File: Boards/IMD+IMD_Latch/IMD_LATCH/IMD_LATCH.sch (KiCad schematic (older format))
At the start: 28 parts

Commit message: hopefully one of the last schematic pushes
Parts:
- removed C?: C_22uF, footprints:C_1206_OEM, symbol Formula:C_22uF
- removed R? (x2): R_604K, footprints:R_0805_OEM, symbol Formula:R_604K
- removed R? (x2): R_2.2K, footprints:R_0805_OEM, symbol Formula:R_2.2K
- removed R?: R_300K, footprints:R_0805_OEM, symbol Formula:R_300K
- removed U?: TLV3701QDBVRG4Q1, footprints:SOT-23-5_OEM, symbol Formula:TLV3701QDBVRG4Q1
- added C1: C_2.2uF, footprints:C_0603_1608Metric, symbol formula:C_2.2uF
- added J1: UF_5_VT, symbol formula:UF_5_VT
- added R7: R_1.82M, footprints:R_0805_OEM, symbol formula:R_1.82M
- C2: renamed from C?; symbol Formula:C_10uF_16V -> IMD_LATCH-rescue:C_10uF_16V-Formula
- D1: renamed from D?; symbol Formula:D_Zener_18V -> IMD_LATCH-rescue:D_Zener_18V-Formula
- D2, D4: renamed from D?; symbol Formula:LED_0805 -> IMD_LATCH-rescue:LED_0805-Formula
- F1: renamed from F?; symbol Formula:F_500mA_16V -> IMD_LATCH-rescue:F_500mA_16V-Formula
- J2: renamed from J?; symbol Formula:MM_F_RA_04 -> IMD_LATCH-rescue:MM_F_RA_04-Formula
- J3: renamed from J?; symbol Formula:MicroFit_V_2 -> IMD_LATCH-rescue:MicroFit_V_2-Formula
- K1: renamed from K?; symbol Formula:G5Q-1A4-DC5-5V -> IMD_LATCH-rescue:G5Q-1A4-DC5-5V-Formula
- Q1, Q2: renamed from Q?; symbol Formula:SSM3K333R -> IMD_LATCH-rescue:SSM3K333R-Formula
- R1: renamed from R?; symbol Formula:R_2.2K -> IMD_LATCH-rescue:R_2.2K-Formula
- R2: renamed from R?; symbol Formula:R_300K -> IMD_LATCH-rescue:R_300K-Formula
- R3, R8: renamed from R?; symbol Formula:R_604K -> IMD_LATCH-rescue:R_604K-Formula
- R4, R5, R9: renamed from R?; symbol Formula:R_1K -> IMD_LATCH-rescue:R_1K-Formula
- R6: renamed from R?; symbol Formula:R_120K -> IMD_LATCH-rescue:R_120K-Formula
- U1: renamed from U?; symbol Formula:TLV3701QDBVRG4Q1 -> IMD_LATCH-rescue:TLV3701QDBVRG4Q1-Formula
- U2: renamed from U?; symbol Formula:CD4043BPWR -> IMD_LATCH-rescue:CD4043BPWR-Formula
- gave numbers to parts that had none: 1
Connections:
- net labels added: IMD_Output
- net labels removed: imd_side_out
- wire segments 79 -> 68
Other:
- note removed: "8V Output"
- note removed: "IMD Output\n"
- moved on the sheet: U1

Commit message: Begin Layout
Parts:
- removed U2: CD4043BPWR, footprints:TSSOP-16-OEM, symbol IMD_LATCH-rescue:CD4043BPWR-Formula
- added C3, C4: C_0.1uF, footprints:C_0805_OEM, symbol footprints:C_0.1uF
- added R10: R_2.2K, footprints:R_0805_OEM, symbol formula:R_2.2K
- added R11: R_2.2K, footprints:R_0805_OEM, symbol IMD_LATCH-rescue:R_2.2K-Formula
- added R12: R_300K, footprints:R_0805_OEM, symbol IMD_LATCH-rescue:R_300K-Formula
- added R13: R_604K, footprints:R_0805_OEM, symbol IMD_LATCH-rescue:R_604K-Formula
- added U2: CD4043BPWR, footprints:TSSOP-16-OEM, symbol formula:CD4043BPWR
- added U3: TLV3701QDBVRG4Q1, footprints:SOT-23-5_OEM, symbol formula:TLV3701QDBVRG4Q1
- D3: footprint (none) -> footprints:D_0805_OEM
- J1: footprint (none) -> footprints:Ultrafit_5
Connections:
- net +12V: no longer D1.1 (K)
- net 12V_Fused: now also D1.1 (K), C3.2, C4.2, R11.2, U2.16 (Vdd), U2.5 (ENABLE), U3.5 (V+)
- net GND: now also C3.1, C4.1, R10.2, R13.1, U2.11 (R3), U2.12 (S3), U2.14 (S4), U2.15 (R4), U2.6 (S2), U2.7 (R2), U2.8 (Vss), U3.2 (V-)
- net IMD_Output: now also R10.1, U3.1 (+)
- net IMD_Status_Output: now also U2.13 (Q1)
- net delay_side_out: no longer names the net of U1.4
- net delay_side_out: now also U2.3 (R1)
- new net: R12.1, R13.2, U3.3 (-)
- new net: U2.4 (S1), U3.4
- new net: R11.1, R12.2
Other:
- note added: "10V Output in 4.2 Sec delay\n"
- note added: "DELAY SIDE:\ntimer gives the IMD time to power up"
- note added: "I _lim: 20mA\n"
- note added: "INPUT CONNECTOR\n\n"
- note added: "Latch outputs 12V when the IMD Output is “Healthy”"
- note added: "POWER MANAGEMENT / FUSING\n\n"
- note added: "This is IMD\n\n"
- note added: "“GOOD” Output is Logical High in a range of 0V-12V; Threshold set to +8V\n"
- note removed: "10V Output\napprox. 4.2 Sec delay\n"
- note removed: "8V output\n"
- note removed: "Comparator outputs12V when the IMD Output is "Healthy""
- note removed: "Delay Side\nA delay to give the IMD time to power up"
- note removed: "HealthyIMD Output is "High" in a range of 0V-12V.\nSo 8V had been chosen as the lower limit of the IMD output\n"
- note removed: "Input, Output and Fuses the 12V\n"
- note removed: "current: 20mA\n"
- note removed: "no Ultrafit_5(IMD)\n\n"
- moved on the sheet: C1, C2, D1, D2, D3, D4, F1, J1, J2, J3, K1, Q1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

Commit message: Revert "Begin Layout"
This reverts commit f66e97611986f6cb10e89dffa2fa205961dd2a3d.
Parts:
- removed C3, C4: C_0.1uF, footprints:C_0805_OEM, symbol footprints:C_0.1uF
- removed R10: R_2.2K, footprints:R_0805_OEM, symbol formula:R_2.2K
- removed R11: R_2.2K, footprints:R_0805_OEM, symbol IMD_LATCH-rescue:R_2.2K-Formula
- removed R12: R_300K, footprints:R_0805_OEM, symbol IMD_LATCH-rescue:R_300K-Formula
- removed R13: R_604K, footprints:R_0805_OEM, symbol IMD_LATCH-rescue:R_604K-Formula
- removed U2: CD4043BPWR, footprints:TSSOP-16-OEM, symbol formula:CD4043BPWR
- removed U3: TLV3701QDBVRG4Q1, footprints:SOT-23-5_OEM, symbol formula:TLV3701QDBVRG4Q1
- added U2: CD4043BPWR, footprints:TSSOP-16-OEM, symbol IMD_LATCH-rescue:CD4043BPWR-Formula
- D3: footprint footprints:D_0805_OEM -> (none)
- J1: footprint footprints:Ultrafit_5 -> (none)
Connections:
- net +12V: now also D1.1 (K)
- net 12V_Fused: now also U2.16 (Vdd), U2.5 (ENABLE); no longer D1.1 (K)
- net GND: now also U2.11 (R3), U2.12 (S3), U2.14 (S4), U2.15 (R4), U2.6 (S2), U2.7 (R2), U2.8 (Vss)
- net IMD_Output: now also U2.4 (S1)
- net IMD_Status_Output: now also U2.13 (NC)
- net delay_side_out: now reaches U1.4
- net delay_side_out: now also U2.3 (R1)
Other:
- note added: "10V Output\napprox. 4.2 Sec delay\n"
- note added: "8V output\n"
- note added: "Comparator outputs12V when the IMD Output is "Healthy""
- note added: "Delay Side\nA delay to give the IMD time to power up"
- note added: "HealthyIMD Output is "High" in a range of 0V-12V.\nSo 8V had been chosen as the lower limit of the IMD output\n"
- note added: "Input, Output and Fuses the 12V\n"
- note added: "current: 20mA\n"
- note added: "no Ultrafit_5(IMD)\n\n"
- note removed: "10V Output in 4.2 Sec delay\n"
- note removed: "DELAY SIDE:\ntimer gives the IMD time to power up"
- note removed: "I _lim: 20mA\n"
- note removed: "INPUT CONNECTOR\n\n"
- note removed: "Latch outputs 12V when the IMD Output is “Healthy”"
- note removed: "POWER MANAGEMENT / FUSING\n\n"
- note removed: "This is IMD\n\n"
- note removed: "“GOOD” Output is Logical High in a range of 0V-12V; Threshold set to +8V\n"
- moved on the sheet: C1, C2, D1, D2, D3, D4, F1, J1, J2, J3, K1, Q1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

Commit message: IMD push
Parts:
- added R?: R_2.2K, footprints:R_0805_OEM, symbol formula:R_2.2K
- added U?: TLV3701QDBVRG4Q1, footprints:SOT-23-5_OEM, symbol formula:TLV3701QDBVRG4Q1
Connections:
- net GND: now also R?.2
- net IMD_Output: now also R?.1, U?.1 (+); no longer U2.4 (S1)
- net 8v_output: now reaches R2.1, R3.2, U1.3 (-)
- net 8v_output: now also U?.3 (-)
- new net IMD_Side_Output: U2.4 (S1), U?.4
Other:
- note removed: "8V output\n"
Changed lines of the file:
@@
 Text Label 5700 3050 2    50   ~ 0
 delay_side_out
-Text Label 5700 3150 2    50   ~ 0
-IMD_Output
 $Comp
 L power:GND #PWR015
@@
 	1    0    0    -1
 $EndComp
-Wire Wire Line
-	1100 4400 1050 4400
-Text Label 1100 4400 0    50   ~ 0
-IMD_Output
 $Comp
 L power:GND #PWR07
@@
 Text Notes 600  700  0    50   ~ 0
 Delay Side\nA delay to give the IMD time to power up
-Text Notes 900  2150 0    50   ~ 0
-8V output\n
 $Comp
 L power:GND #PWR01
@@
 $EndComp
 Connection ~ 1550 1000
+$Comp
+L formula:R_2.2K R?
+U 1 1 5DEA1AC3
+P 1850 4550
+F 0 "R?" H 1920 4596 50  0000 L CNN
+F 1 "R_2.2K" H 1920 4505 50  0000 L CNN
+F 2 "footprints:R_0805_OEM" H 1780 4550 50  0001 C CNN
+F 3 "https://www.seielect.com/Catalog/SEI-RMCF_RMCP.pdf" H 1930 4550 50  0001 C CNN
+F 4 "DK" H 1850 4550 60  0001 C CNN "MFN"
+F 5 "RMCF0805FT2K20CT-ND" H 1850 4550 60  0001 C CNN "MPN"
+F 6 "https://www.digikey.com/product-detail/en/stackpole-electronics-inc/RMCF0805FT2K20/RMCF0805FT2K20CT-ND/1942387" H 2330 4950 60  0001 C CNN "PurchasingLink"
+	1    1850 4550
+	1    0    0    -1
+$EndComp
+$Comp
+L formula:TLV3701QDBVRG4Q1 U?
+U 1 1 5DEA27E2
+P 2950 4500
+F 0 "U?" H 3294 4664 50  0000 L CNN
+F 1 "TLV3701QDBVRG4Q1" H 3294 4731 50  0000 L CNN
+F 2 "footprints:SOT-23-5_OEM" H 2950 4600 50  0001 C CNN
+F 3 "http://www.ti.com/lit/ds/symlink/tlv3702-q1.pdf" H 2950 4700 50  0001 C CNN
+F 4 "DK" H 3300 5000 60  0001 C CNN "MFN"
+F 5 "497-10249-1-ND" H 3200 4900 60  0001 C CNN "MPN"
+F 6 "https://www.digikey.com/product-detail/en/texas-instruments/TLV3701QDBVRG4Q1/296-32395-6-ND/3507000" H 3100 4800 60  0001 C CNN "PurchasingLink"
+	1    2950 4500
+	1    0    0    -1
+$EndComp
+Wire Wire Line
+	1050 4400 1850 4400
+Wire Wire Line
+	2650 4400 1850 4400
+Connection ~ 1850 4400
+$Comp
+L power:GND #PWR?
+U 1 1 5DEA844C
+P 1850 4700
+F 0 "#PWR?" H 1850 4450 50  0001 C CNN
+F 1 "GND" H 1855 4527 50  0000 C CNN
+F 2 "" H 1850 4700 50  0001 C CNN
+F 3 "" H 1850 4700 50  0001 C CNN
+	1    1850 4700
+	1    0    0    -1
+$EndComp
+Text Label 2650 4600 2    50   ~ 0
+8v_output
+Text Label 650  2150 0    50   ~ 0
+8v_output
+Text Label 3250 4500 0    50   ~ 0
+IMD_Side_Output
+Text Label 5700 3150 2    50   ~ 0
+IMD_Side_Output
+Text Label 1050 4400 0    50   ~ 0
+IMD_Output
 $EndSCHEMATC

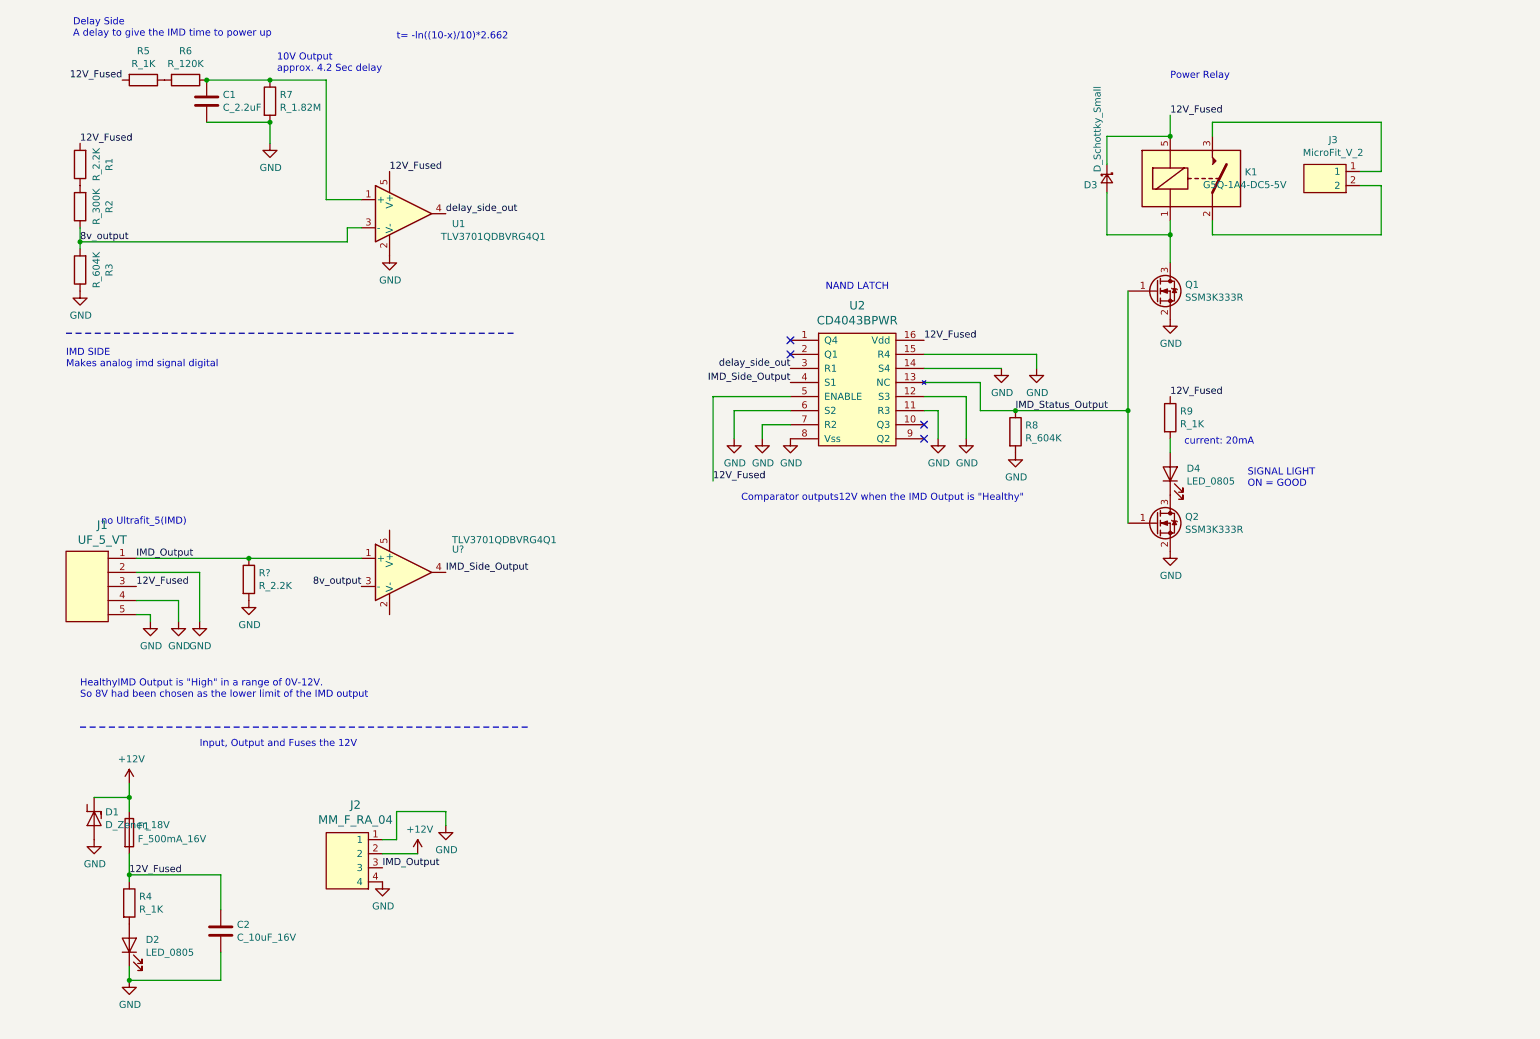
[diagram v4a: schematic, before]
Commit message: Fixed IMD Latch Schematic + Finished Layout
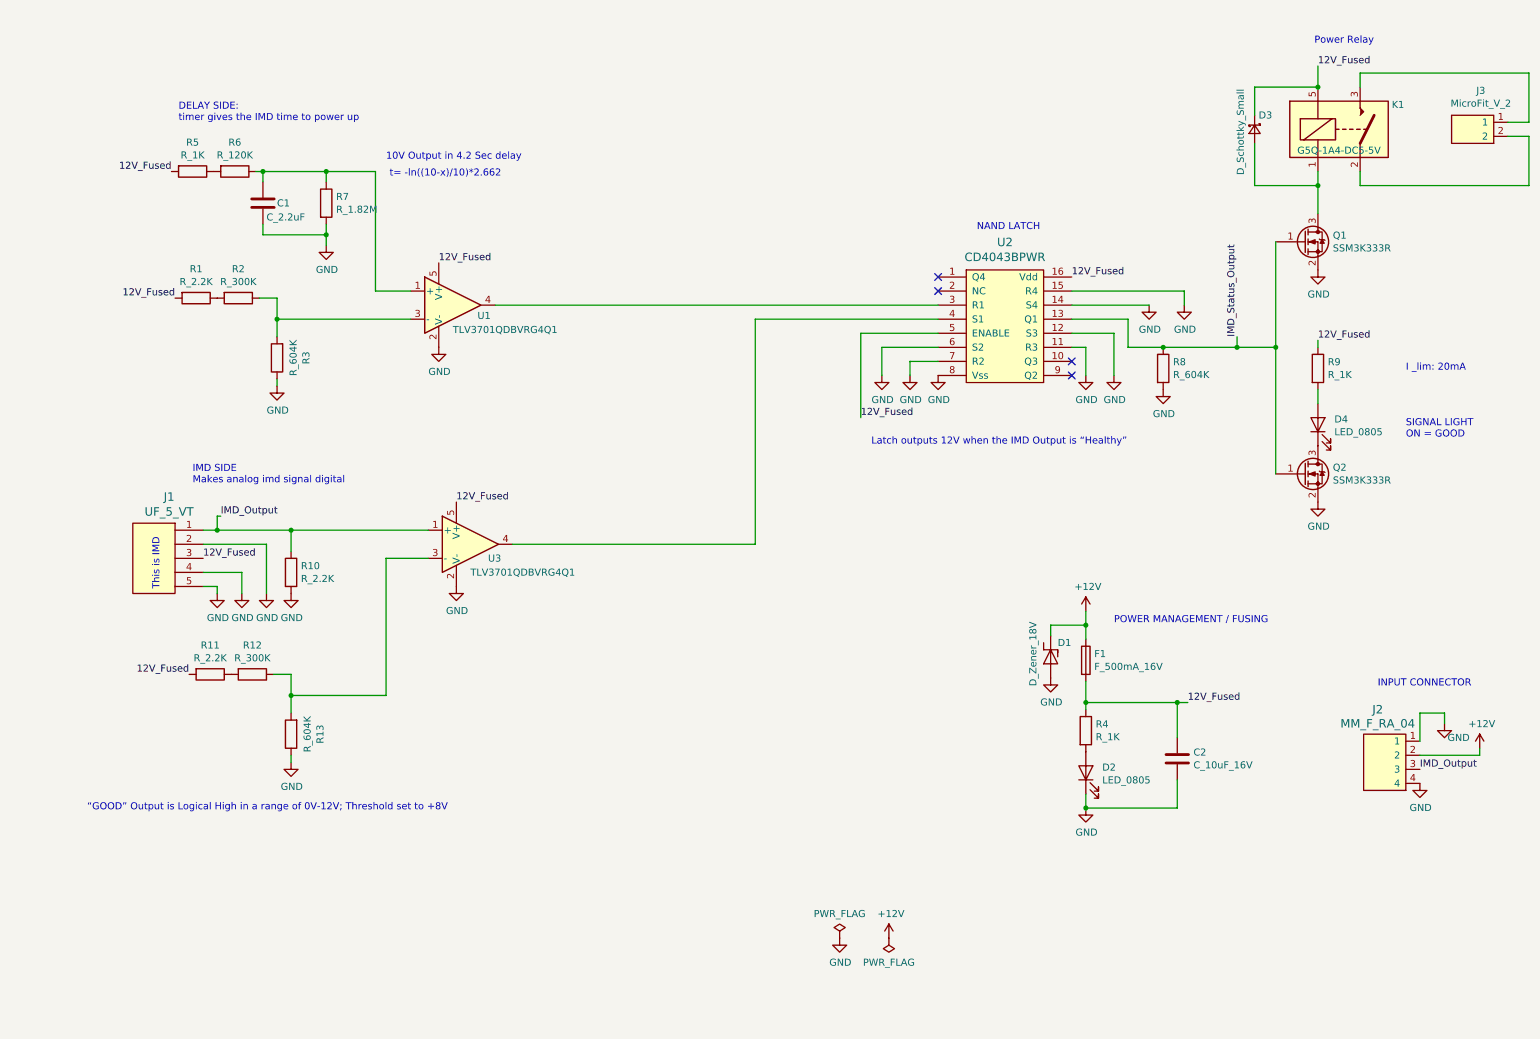
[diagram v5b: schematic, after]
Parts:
- removed U2: CD4043BPWR, footprints:TSSOP-16-OEM, symbol IMD_LATCH-rescue:CD4043BPWR-Formula
- added R11: R_2.2K, footprints:R_0805_OEM, symbol IMD_LATCH-rescue:R_2.2K-Formula
- added R12: R_300K, footprints:R_0805_OEM, symbol IMD_LATCH-rescue:R_300K-Formula
- added R13: R_604K, footprints:R_0805_OEM, symbol IMD_LATCH-rescue:R_604K-Formula
- added U2: CD4043BPWR, footprints:TSSOP-16-OEM, symbol formula:CD4043BPWR
- D3: footprint (none) -> footprints:D_0805_OEM
- J1: footprint (none) -> footprints:Ultrafit_5
- gave numbers to parts that had none: 2
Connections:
- net 12V_Fused: now also U3.5 (V+), R11.2, U2.16 (Vdd), U2.5 (ENABLE)
- net GND: now also U3.2 (V-), R13.1, U2.11 (R3), U2.12 (S3), U2.14 (S4), U2.15 (R4), U2.6 (S2), U2.7 (R2), U2.8 (Vss)
- net IMD_Status_Output: now also U2.13 (Q1)
- net 8v_output: no longer names the net of R2.1, R3.2, U1.3 (-)
- net 8v_output: no longer U3.3 (-)
- net IMD_Side_Output: no longer names the net of U3.4
- net IMD_Side_Output: now also U2.4 (S1)
- net delay_side_out: no longer names the net of U1.4
- net delay_side_out: now also U2.3 (R1)
- new net: R12.1, R13.2, U3.3 (-)
- new net: R11.1, R12.2
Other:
- note added: "10V Output in 4.2 Sec delay\n"
- note added: "DELAY SIDE:\ntimer gives the IMD time to power up"
- note added: "I _lim: 20mA\n"
- note added: "INPUT CONNECTOR\n\n"
- note added: "Latch outputs 12V when the IMD Output is “Healthy”"
- note added: "POWER MANAGEMENT / FUSING\n\n"
- note added: "This is IMD\n\n"
- note added: "“GOOD” Output is Logical High in a range of 0V-12V; Threshold set to +8V\n"
- note removed: "10V Output\napprox. 4.2 Sec delay\n"
- note removed: "Comparator outputs12V when the IMD Output is "Healthy""
- note removed: "Delay Side\nA delay to give the IMD time to power up"
- note removed: "HealthyIMD Output is "High" in a range of 0V-12V.\nSo 8V had been chosen as the lower limit of the IMD output\n"
- note removed: "Input, Output and Fuses the 12V\n"
- note removed: "current: 20mA\n"
- note removed: "no Ultrafit_5(IMD)\n\n"
- moved on the sheet: C1, C2, D1, D2, D3, D4, F1, J1, J2, J3, K1, Q1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
